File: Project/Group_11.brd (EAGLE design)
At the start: 29 parts, among them J1 POWER_JACKPTH_LOCK, U1 +12v

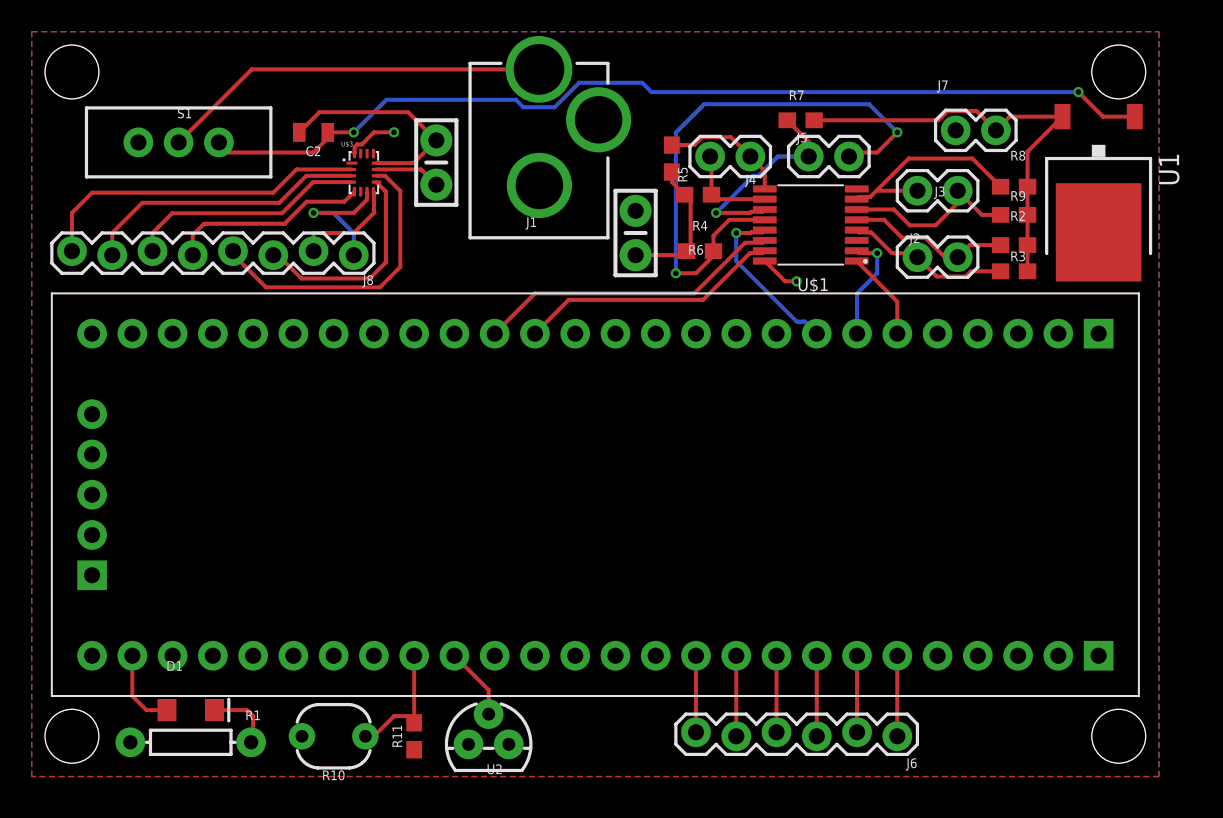
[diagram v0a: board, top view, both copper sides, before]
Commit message: Versione corretta con path da 8 mil nel mux, holes da 3mm
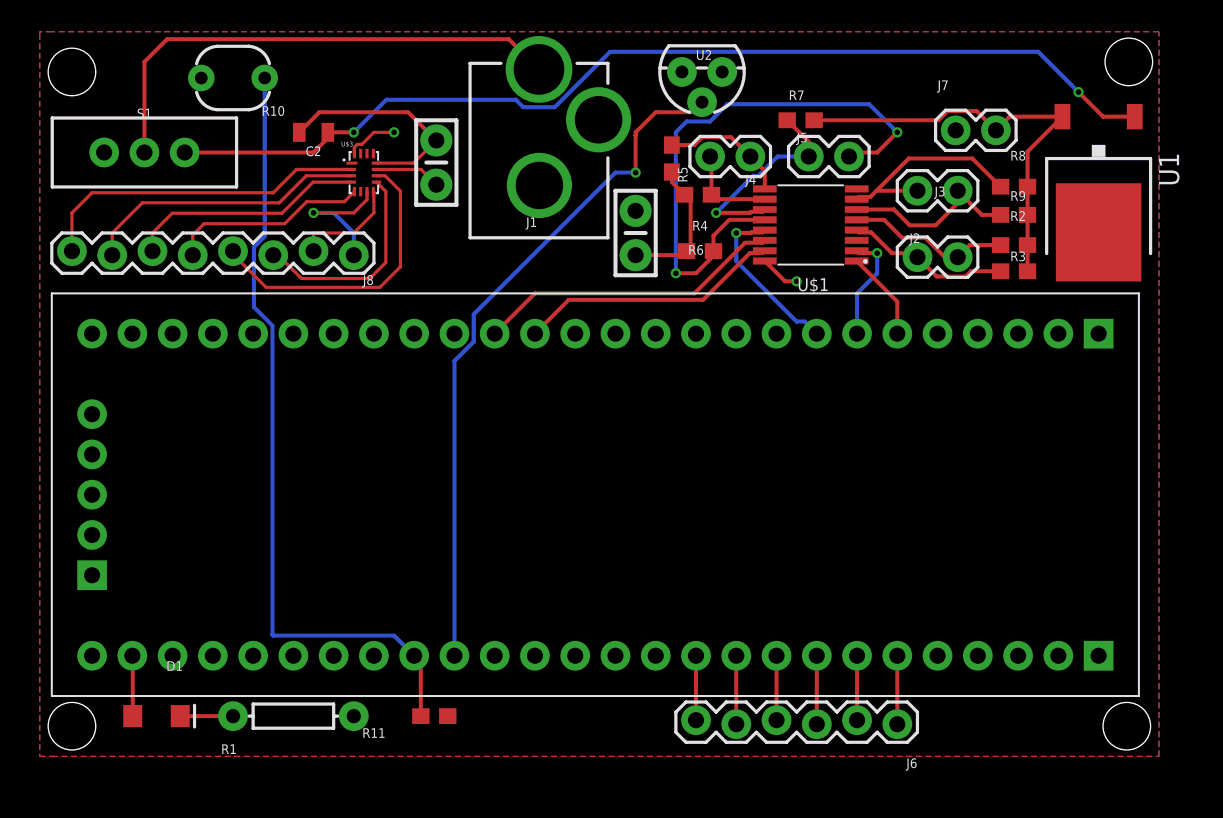
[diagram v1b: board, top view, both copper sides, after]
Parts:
- moved U2 44.5 mm to (42.3, 44.5), turned to 180 degrees
- moved R10 42.0 mm to (12.7, 44.1)
- moved R1 6.68 mm to (16.5, 3.81), turned to 180 degrees
- moved S1 2.25 mm to (7.11, 39.4)
- moved D1 2.19 mm to (7.87, 3.81)
- moved R11 1.80 mm to (25.4, 3.81), turned to 180 degrees
- moved J6 0.76 mm to (54.6, 3.30)
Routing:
- net PHOTO_OUT: track 8.01 -> 49.4 mm
- net TEMP_OUT: track 4.58 -> 43.5 mm, vias 0 -> 1
- net N$9: track 24.6 -> 32.0 mm
- net 12V: track 61.4 -> 64.9 mm
- net N$3: track 5.09 -> 3.82 mm
- net N$2: track 4.30 -> 3.33 mm
- net N$8: track 4.83 -> 4.06 mm
- net N$7: track 5.08 -> 4.32 mm
- net N$6: track 4.83 -> 4.06 mm
- net N$5: track 5.08 -> 4.32 mm
- net N$4: track 4.83 -> 4.06 mm
- net N$17: track 5.08 -> 4.32 mm

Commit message: Board senza errori
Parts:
- moved R4 1.02 mm to (41.9, 35.7), turned to 270 degrees
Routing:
- net I2C_SCL_2: track 5.93 -> 7.33 mm
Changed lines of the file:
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@@
 <attribute name="VALUE" x="62.23" y="30.988" size="0.6096" layer="27" font="vector" ratio="20" align="top-center"/>
 </element>
-<element name="R4" library="SparkFun-Resistors" package="0603" value="4.7k" x="42.037" y="36.703" smashed="yes" rot="R180">
-<attribute name="NAME" x="42.164" y="35.052" size="0.6096" layer="25" font="vector" ratio="20" rot="R180" align="bottom-center"/>
-<attribute name="PROD_ID" value="RES-07857" x="-21.336" y="86.614" size="1.778" layer="27" rot="R180" display="off"/>
-<attribute name="VALUE" x="42.164" y="36.576" size="0.6096" layer="27" font="vector" ratio="20" rot="R180" align="top-center"/>
+<element name="R4" library="SparkFun-Resistors" package="0603" value="4.7k" x="41.91" y="35.687" smashed="yes" rot="R270">
+<attribute name="NAME" x="43.688" y="37.084" size="0.6096" layer="25" font="vector" ratio="20" rot="R270" align="bottom-center"/>
+<attribute name="PROD_ID" value="RES-07857" x="-7.874" y="-26.416" size="1.778" layer="27" rot="R270" display="off"/>
+<attribute name="VALUE" x="42.164" y="37.084" size="0.6096" layer="27" font="vector" ratio="20" rot="R270" align="top-center"/>
 </element>
 <element name="R5" library="SparkFun-Resistors" package="0603" value="4.7k" x="40.386" y="38.989" smashed="yes" rot="R270">
@@
 <wire x1="65.03" y1="41.63" x2="61.696" y2="41.63" width="0.254" layer="1"/>
 <wire x1="61.696" y1="41.63" x2="60.833" y2="40.767" width="0.254" layer="1"/>
-<wire x1="41.568" y1="36.322" x2="41.568" y2="33.401" width="0.254" layer="1"/>
-<wire x1="41.314" y1="33.147" x2="41.568" y2="33.401" width="0.254" layer="1"/>
-<wire x1="41.568" y1="36.322" x2="41.187" y2="36.703" width="0.254" layer="1"/>
 <wire x1="49.364" y1="41.402" x2="57.2037875" y2="41.402" width="0.254" layer="1"/>
 <wire x1="57.2037875" y1="41.402" x2="57.7879875" y2="41.9862" width="0.254" layer="1"/>
 <wire x1="57.7879875" y1="41.9862" x2="59.6138" y2="41.9862" width="0.254" layer="1"/>
 <wire x1="59.6138" y1="41.9862" x2="60.833" y2="40.767" width="0.254" layer="1"/>
-<wire x1="40.386" y1="37.504" x2="40.386" y2="38.139" width="0.254" layer="1"/>
-<wire x1="41.187" y1="36.703" x2="40.386" y2="37.504" width="0.254" layer="1"/>
 <wire x1="21.755" y1="38.3" x2="24.56501875" y2="38.3" width="0.2032" layer="1"/>
 <wire x1="24.56501875" y1="38.3" x2="25.527" y2="37.338" width="0.2032" layer="1"/>
@@
 <wire x1="20.355" y1="39.3" x2="20.355" y2="39.69513125" width="0.2032" layer="1"/>
 <wire x1="20.355" y1="39.69513125" x2="20.53926875" y2="39.8794" width="0.2032" layer="1"/>
+<wire x1="41.91" y1="34.837" x2="40.386" y2="36.361" width="0.254" layer="1"/>
+<wire x1="40.386" y1="36.361" x2="40.386" y2="38.139" width="0.254" layer="1"/>
+<wire x1="41.314" y1="33.147" x2="41.314" y2="34.241" width="0.254" layer="1"/>
+<wire x1="41.314" y1="34.241" x2="41.91" y2="34.837" width="0.254" layer="1"/>
 </signal>
 <signal name="N$9">
@@
 <contactref element="U$1" pad="10"/>
 <contactref element="R4" pad="1"/>
-<wire x1="42.887" y1="36.703" x2="43.167" y2="36.423" width="0.254" layer="1"/>
-<wire x1="43.167" y1="36.423" x2="46.249" y2="36.423" width="0.254" layer="1"/>
-<wire x1="42.887" y1="36.703" x2="42.887" y2="39.028" width="0.254" layer="1"/>
-<wire x1="42.887" y1="39.028" x2="42.799" y2="39.116" width="0.254" layer="1"/>
+<wire x1="41.91" y1="36.537" x2="41.91" y2="38.227" width="0.254" layer="1"/>
+<wire x1="41.91" y1="38.227" x2="42.799" y2="39.116" width="0.254" layer="1"/>
+<wire x1="46.249" y1="36.423" x2="42.024" y2="36.423" width="0.254" layer="1"/>
+<wire x1="42.024" y1="36.423" x2="41.91" y2="36.537" width="0.254" layer="1"/>
 </signal>
 <signal name="I2C_SDA_2">

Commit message: Correzione schematico collegamenti MUX
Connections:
- removed net MUX_A0/1.3C: U$3.15
- removed net MUX_A0/2.3C: U$2.24
- removed net MUX_A1/1.4C: U$3.14
- removed net MUX_A1/2.3C: U$2.23
- removed net MUX_A2/1.4C: U$3.13
- removed net MUX_A2/2.3C: U$2.22
- removed net MUX_OUT/1.4C: U$3.6
- removed net MUX_OUT/2.5C: U$2.21
- new net MUX_A0: U$2.24, U$3.15
- new net MUX_A1: U$2.23, U$3.14
- new net MUX_A2: U$2.22, U$3.13
- new net MUX_OUT: U$2.21, U$3.6
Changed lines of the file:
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@@
 <wire x1="36.83" y1="38.1" x2="38.1" y2="38.1" width="0.254" layer="16"/>
-</signal>
-<signal name="MUX_A0/2.3C">
-<contactref element="U$2" pad="24"/>
-</signal>
-<signal name="MUX_A1/2.3C">
-<contactref element="U$2" pad="23"/>
-</signal>
-<signal name="MUX_A2/2.3C">
-<contactref element="U$2" pad="22"/>
-</signal>
-<signal name="MUX_OUT/2.5C">
-<contactref element="U$2" pad="21"/>
 </signal>
 <signal name="I2C_A2">
@@
 <wire x1="17.7547375" y1="37.5" x2="15.7893375" y2="35.5346" width="0.2032" layer="1"/>
 </signal>
-<signal name="MUX_OUT/1.4C">
+<signal name="MUX_OUT">
 <contactref element="U$3" pad="6"/>
-</signal>
-<signal name="MUX_A0/1.3C">
+<contactref element="U$2" pad="21"/>
+<wire x1="16.51" y1="27.94" x2="20.755" y2="36.9" width="0" layer="19" extent="1-1"/>
+</signal>
+<signal name="MUX_A0">
 <contactref element="U$3" pad="15"/>
-</signal>
-<signal name="MUX_A1/1.4C">
+<contactref element="U$2" pad="24"/>
+<wire x1="8.89" y1="27.94" x2="20.755" y2="39.3" width="0" layer="19" extent="1-1"/>
+</signal>
+<signal name="MUX_A1">
 <contactref element="U$3" pad="14"/>
-</signal>
-<signal name="MUX_A2/1.4C">
+<contactref element="U$2" pad="23"/>
+<wire x1="11.43" y1="27.94" x2="21.155" y2="39.3" width="0" layer="19" extent="1-1"/>
+</signal>
+<signal name="MUX_A2">
 <contactref element="U$3" pad="13"/>
+<contactref element="U$2" pad="22"/>
+<wire x1="13.97" y1="27.94" x2="21.555" y2="39.3" width="0" layer="19" extent="1-1"/>
 </signal>
 </signals>

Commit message: Aggiunta collegamenti board
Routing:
- net MUX_A0: track 0.00 -> 54.9 mm, vias 0 -> 2
- net MUX_A1: track 0.00 -> 33.5 mm, vias 0 -> 2
- net MUX_A2: track 0.00 -> 17.7 mm, vias 0 -> 2
- net MUX_OUT: track 0.00 -> 11.1 mm, vias 0 -> 1
- net N$11: track 8.69 -> 4.35 mm
- net 5V: track 46.6 -> 44.7 mm
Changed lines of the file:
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@@
 <wire x1="21.755" y1="38.3" x2="24.56501875" y2="38.3" width="0.2032" layer="1"/>
 <wire x1="24.56501875" y1="38.3" x2="25.527" y2="37.338" width="0.2032" layer="1"/>
-<wire x1="20.53926875" y1="39.8794" x2="20.8294" y2="39.8794" width="0.2032" layer="1"/>
-<wire x1="20.8294" y1="39.8794" x2="21.59" y2="40.64" width="0.2032" layer="1"/>
-<wire x1="21.59" y1="40.64" x2="22.86" y2="40.64" width="0.2032" layer="1"/>
-<via x="22.86" y="40.64" extent="1-16" drill="0.35"/>
+<via x="19.05" y="39.37" extent="1-16" drill="0.35"/>
 <wire x1="41.314" y1="33.147" x2="41.06" y2="32.893" width="0.254" layer="1"/>
 <wire x1="41.06" y1="32.893" x2="38.1" y2="32.893" width="0.254" layer="1"/>
@@
 <vertex x="0.508" y="1.27"/>
 </polygon>
-<wire x1="20.355" y1="39.3" x2="20.355" y2="39.69513125" width="0.2032" layer="1"/>
-<wire x1="20.355" y1="39.69513125" x2="20.53926875" y2="39.8794" width="0.2032" layer="1"/>
 <wire x1="41.91" y1="34.837" x2="40.386" y2="36.361" width="0.254" layer="1"/>
 <wire x1="40.386" y1="36.361" x2="40.386" y2="38.139" width="0.254" layer="1"/>
 <wire x1="41.314" y1="33.147" x2="41.314" y2="34.241" width="0.254" layer="1"/>
 <wire x1="41.314" y1="34.241" x2="41.91" y2="34.837" width="0.254" layer="1"/>
+<wire x1="20.355" y1="39.3" x2="19.12" y2="39.3" width="0.1524" layer="1"/>
+<wire x1="19.12" y1="39.3" x2="19.05" y2="39.37" width="0.1524" layer="1"/>
 </signal>
 <signal name="N$9">
@@
 <contactref element="J8" pad="1"/>
 <contactref element="U$3" pad="7"/>
-<wire x1="20.32" y1="35.56" x2="17.78" y2="35.56" width="0.2032" layer="1"/>
-<via x="17.78" y="35.56" extent="1-16" drill="0.35"/>
-<wire x1="17.78" y1="35.56" x2="19.05" y2="35.56" width="0.254" layer="16"/>
-<wire x1="19.05" y1="35.56" x2="20.32" y2="34.29" width="0.254" layer="16"/>
-<wire x1="20.32" y1="34.29" x2="20.32" y2="32.893" width="0.254" layer="16"/>
-<wire x1="21.155" y1="36.9" x2="21.155" y2="36.395" width="0.2032" layer="1"/>
-<wire x1="21.155" y1="36.395" x2="20.32" y2="35.56" width="0.2032" layer="1"/>
+<wire x1="20.32" y1="32.893" x2="20.32" y2="35.56" width="0.1524" layer="16"/>
+<via x="20.32" y="35.56" extent="1-16" drill="0.35"/>
+<wire x1="20.32" y1="35.56" x2="21.155" y2="36.395" width="0.1524" layer="1"/>
+<wire x1="21.155" y1="36.395" x2="21.155" y2="36.9" width="0.1524" layer="1"/>
 </signal>
 <signal name="N$12">
@@
 <contactref element="U$3" pad="6"/>
 <contactref element="U$2" pad="21"/>
-<wire x1="16.51" y1="27.94" x2="20.755" y2="36.9" width="0" layer="19" extent="1-1"/>
+<wire x1="16.51" y1="27.94" x2="19.05" y2="30.48" width="0.1524" layer="16"/>
+<wire x1="19.05" y1="30.48" x2="19.05" y2="35.56" width="0.1524" layer="16"/>
+<via x="19.05" y="35.56" extent="1-16" drill="0.35"/>
+<wire x1="19.05" y1="35.56" x2="19.4248" y2="35.9348" width="0.1524" layer="1"/>
+<wire x1="19.4248" y1="35.9348" x2="19.856775" y2="35.9348" width="0.1524" layer="1"/>
+<wire x1="20.293375" y1="36.3714" x2="20.5496875" y2="36.3714" width="0.1524" layer="1"/>
+<wire x1="19.856775" y1="35.9348" x2="20.293375" y2="36.3714" width="0.1524" layer="1"/>
+<wire x1="20.6852" y1="36.8302" x2="20.755" y2="36.9" width="0.1524" layer="1"/>
+<wire x1="20.5496875" y1="36.3714" x2="20.6852" y2="36.5069125" width="0.1524" layer="1"/>
+<wire x1="20.6852" y1="36.5069125" x2="20.6852" y2="36.8302" width="0.1524" layer="1"/>
 </signal>
 <signal name="MUX_A0">
 <contactref element="U$3" pad="15"/>
 <contactref element="U$2" pad="24"/>
-<wire x1="8.89" y1="27.94" x2="20.755" y2="39.3" width="0" layer="19" extent="1-1"/>
+<wire x1="8.89" y1="27.94" x2="10.16" y2="26.67" width="0.1524" layer="1"/>
+<wire x1="10.16" y1="26.67" x2="10.16" y2="24.13" width="0.1524" layer="1"/>
+<wire x1="10.16" y1="24.13" x2="25.4" y2="24.13" width="0.1524" layer="1"/>
+<wire x1="25.4" y1="24.13" x2="25.4" y2="34.29" width="0.1524" layer="1"/>
+<wire x1="25.4" y1="34.29" x2="26.67" y2="35.56" width="0.1524" layer="1"/>
+<wire x1="26.67" y1="35.56" x2="27.94" y2="35.56" width="0.1524" layer="1"/>
+<wire x1="27.94" y1="35.56" x2="27.94" y2="43.18" width="0.1524" layer="1"/>
+<wire x1="27.94" y1="43.18" x2="20.32" y2="43.18" width="0.1524" layer="1"/>
+<via x="20.32" y="43.18" extent="1-16" drill="0.35"/>
+<wire x1="19.764" y1="40.87030625" x2="19.764" y2="40.40969375" width="0.1524" layer="16"/>
+<wire x1="19.764" y1="40.40969375" x2="20.08969375" y2="40.084" width="0.1524" layer="16"/>
+<wire x1="20.08969375" y1="40.084" x2="20.55030625" y2="40.084" width="0.1524" layer="16"/>
+<wire x1="20.32" y1="43.18" x2="20.32" y2="41.42630625" width="0.1524" layer="16"/>
+<wire x1="20.32" y1="41.42630625" x2="19.764" y2="40.87030625" width="0.1524" layer="16"/>
+<wire x1="20.55030625" y1="40.084" x2="21.10630625" y2="40.64" width="0.1524" layer="16"/>
+<wire x1="21.10630625" y1="40.64" x2="21.59" y2="40.64" width="0.1524" layer="16"/>
+<via x="21.59" y="40.64" extent="1-16" drill="0.35"/>
+<wire x1="21.59" y1="40.64" x2="20.755" y2="39.805" width="0.1524" layer="1"/>
+<wire x1="20.755" y1="39.805" x2="20.755" y2="39.3" width="0.1524" layer="1"/>
 </signal>
 <signal name="MUX_A1">
 <contactref element="U$3" pad="14"/>
 <contactref element="U$2" pad="23"/>
-<wire x1="11.43" y1="27.94" x2="21.155" y2="39.3" width="0" layer="19" extent="1-1"/>
+<wire x1="11.43" y1="27.94" x2="11.43" y2="25.4" width="0.1524" layer="1"/>
+<wire x1="11.43" y1="25.4" x2="22.86" y2="25.4" width="0.1524" layer="1"/>
+<wire x1="22.86" y1="25.4" x2="22.86" y2="30.48" width="0.1524" layer="1"/>
+<wire x1="22.86" y1="30.48" x2="24.13" y2="31.75" width="0.1524" layer="1"/>
+<wire x1="24.13" y1="31.75" x2="24.13" y2="34.29" width="0.1524" layer="1"/>
+<via x="24.13" y="34.29" extent="1-16" drill="0.35"/>
+<wire x1="24.13" y1="34.29" x2="24.13" y2="40.64" width="0.1524" layer="16"/>
+<wire x1="24.13" y1="40.64" x2="22.86" y2="40.64" width="0.1524" layer="16"/>
+<via x="22.86" y="40.64" extent="1-16" drill="0.35"/>
+<wire x1="21.3603125" y1="39.8286" x2="21.2264" y2="39.6946875" width="0.1524" layer="1"/>
+<wire x1="22.86" y1="40.64" x2="22.0486" y2="39.8286" width="0.1524" layer="1"/>
+<wire x1="21.2264" y1="39.6946875" x2="21.2264" y2="39.3714" width="0.1524" layer="1"/>
+<wire x1="21.2264" y1="39.3714" x2="21.155" y2="39.3" width="0.1524" layer="1"/>
+<wire x1="22.0486" y1="39.8286" x2="21.3603125" y2="39.8286" width="0.1524" layer="1"/>
 </signal>
 <signal name="MUX_A2">
 <contactref element="U$3" pad="13"/>
 <contactref element="U$2" pad="22"/>
-<wire x1="13.97" y1="27.94" x2="21.555" y2="39.3" width="0" layer="19" extent="1-1"/>
+<wire x1="13.97" y1="27.94" x2="15.24" y2="29.21" width="0.1524" layer="1"/>
+<via x="15.24" y="29.21" extent="1-16" drill="0.35"/>
+<wire x1="15.24" y1="29.21" x2="16.6116" y2="30.5816" width="0.1524" layer="16"/>
+<wire x1="16.6116" y1="30.5816" x2="16.6116" y2="33.90790625" width="0.1524" layer="16"/>
+<wire x1="21.555" y1="39.335" x2="21.555" y2="39.3" width="0.1524" layer="1"/>
+<wire x1="16.6116" y1="33.90790625" x2="20.80369375" y2="38.1" width="0.1524" layer="16"/>
+<wire x1="20.80369375" y1="38.1" x2="22.86" y2="38.1" width="0.1524" layer="16"/>
+<wire x1="22.86" y1="38.1" x2="22.86" y2="39.37" width="0.1524" layer="16"/>
+<via x="22.86" y="39.37" extent="1-16" drill="0.35"/>
+<wire x1="22.86" y1="39.37" x2="22.825" y2="39.335" width="0.1524" layer="1"/>
+<wire x1="22.825" y1="39.335" x2="21.555" y2="39.335" width="0.1524" layer="1"/>
 </signal>
 </signals>

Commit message: Correzione clearance
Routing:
- net MUX_A2: track 17.7 -> 22.5 mm, vias 2 -> 1
- net PHOTO_OUT: track 49.4 -> 50.4 mm
- net N$12: track 6.83 -> 7.58 mm
